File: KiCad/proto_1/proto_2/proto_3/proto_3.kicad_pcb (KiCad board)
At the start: 2 copper layers, 10 parts

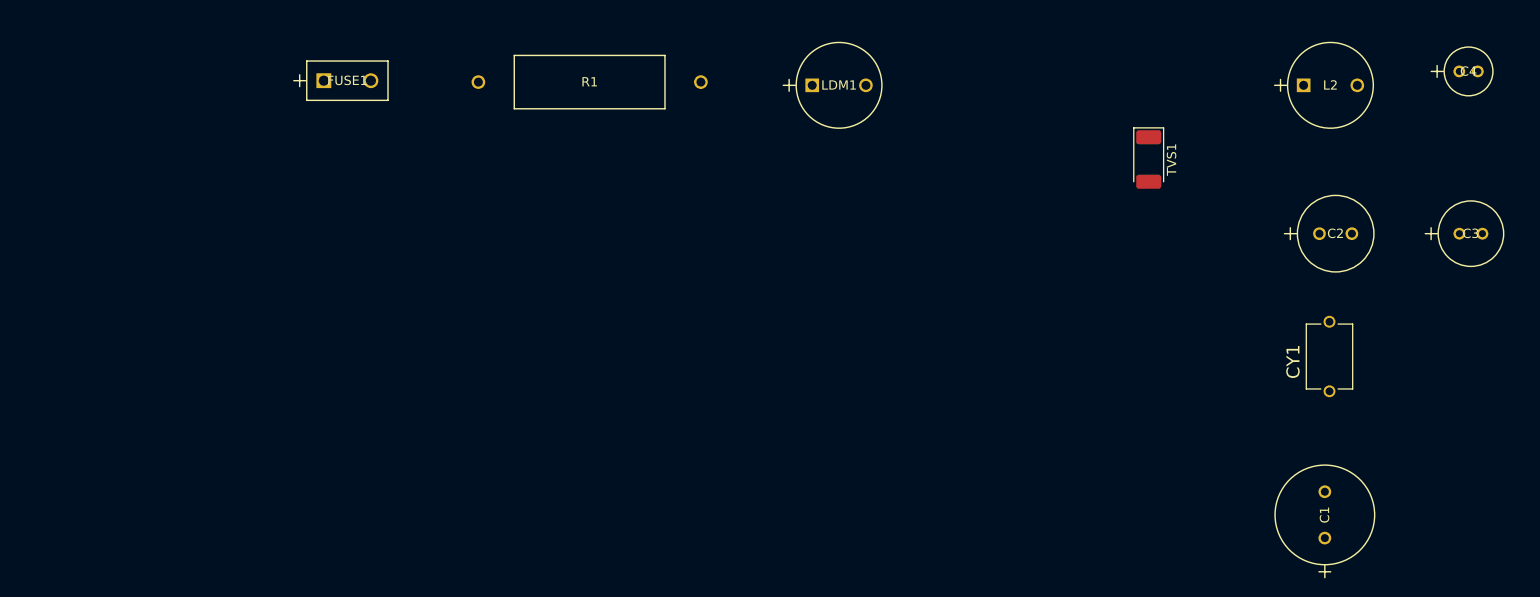
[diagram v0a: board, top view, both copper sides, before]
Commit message: added power symbol, started work on pcb component placement
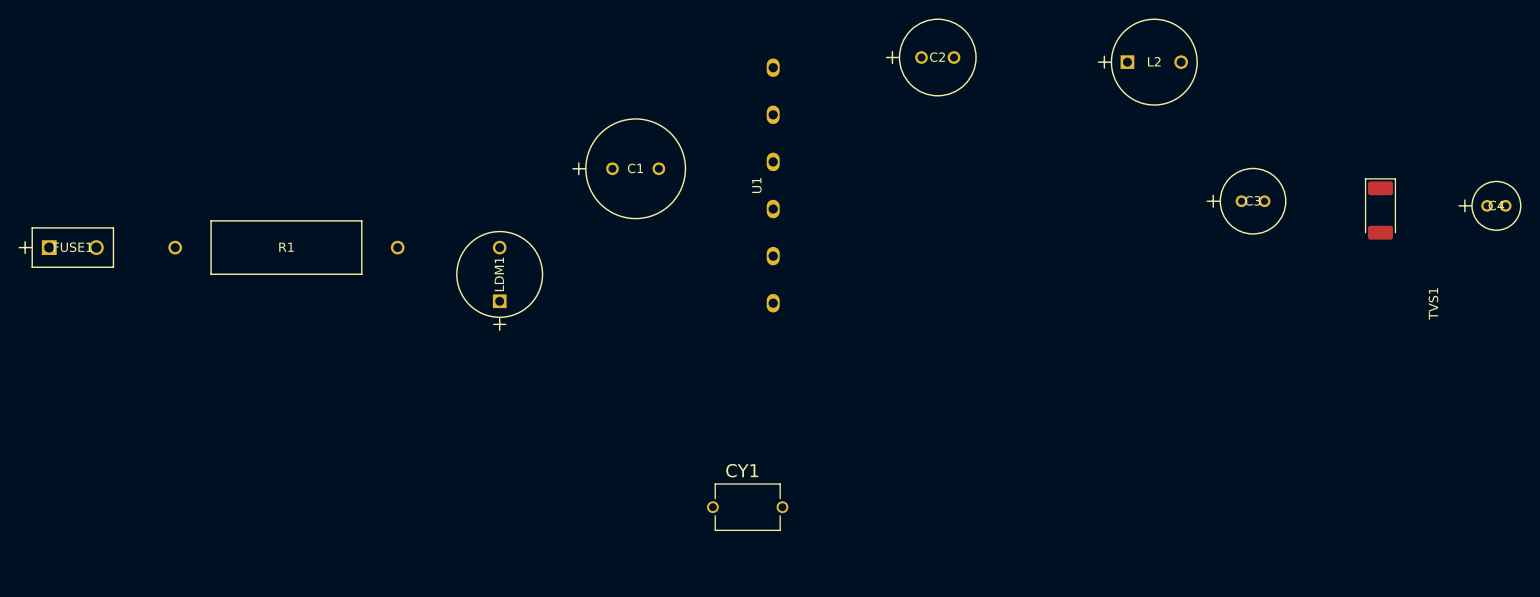
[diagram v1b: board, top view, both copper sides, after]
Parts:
- added U1: ~, stuff:power, F.Cu at (124.0, 88.3)
- moved C1 86.5 mm to (106.7, 86.5), turned to 0 degrees
- moved CY1 64.8 mm to (121.2, 123.0), turned to 0 degrees
- moved C2 46.9 mm to (140.0, 74.5)
- moved LDM1 41.0 mm to (94.5, 100.8), turned to 90 degrees
- moved R1 37.3 mm to (59.5, 95.0)
- moved FUSE1 34.7 mm to (45.9, 95.0)
- moved TVS1 25.6 mm to (189.5, 91.0)
- moved C3 23.8 mm to (174.5, 90.0)
- moved L2 19.2 mm to (162.2, 75.0)
- moved C4 14.8 mm to (201.0, 90.5)
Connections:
- C1 pad 1: unconnected-(C1-Pad1) -> Net-(U1-+V(cap))
- C2 pad 1: Net-(TVS1-A) -> Net-(U1-+Vo)
- C2 pad 2: Net-(C2-Pad2) -> Net-(TVS1-A)
- L2 pad 2: Net-(C2-Pad2) -> Net-(U1-+Vo)
- LDM1 pad 1: unconnected-(LDM1-Pad1) -> Net-(U1-AC(L))
